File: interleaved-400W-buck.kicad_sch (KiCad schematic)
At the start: 3 parts, among them U1 STM32G474CBTx, U2 TCAN330, U3 LTC7891RUFDM

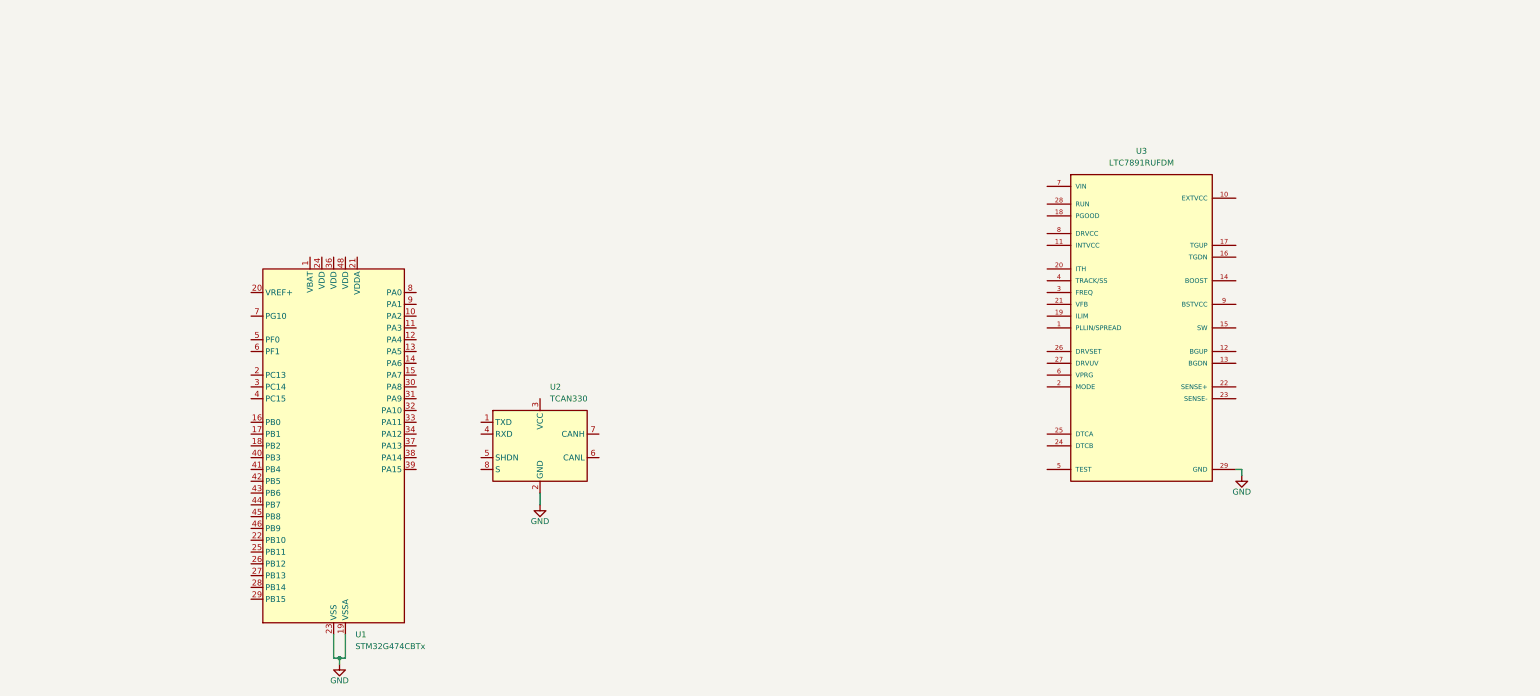
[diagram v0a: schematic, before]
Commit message: Update interleaved-400W-buck.kicad_sch
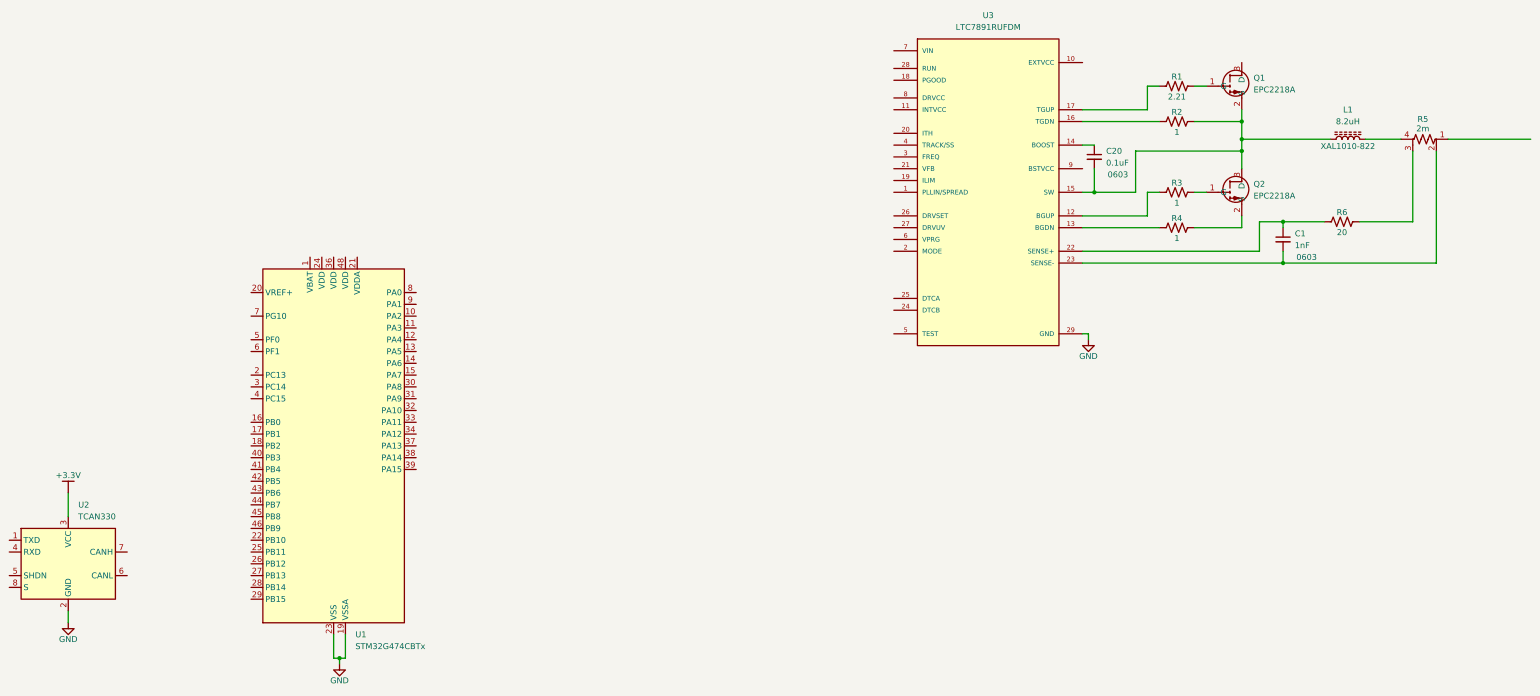
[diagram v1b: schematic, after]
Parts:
- added C1: 1nF, Capacitor_SMD:C_0603_1608Metric_Pad1.08x0.95mm_HandSolder, symbol Device:C_Small
- added C20: 0.1uF, Capacitor_SMD:C_0603_1608Metric_Pad1.08x0.95mm_HandSolder, symbol Device:C_Small
- added L1: 8.2uH, Inductor_SMD:L_Coilcraft_XAL1010-XXX, symbol Device:L_Ferrite
- added Q1, Q2: EPC2218A, jannett_footprints:TRANS_EPC2218A, symbol jannett_symbols:EPC2218A
- added R1: 2.21, Resistor_SMD:R_1206_3216Metric, symbol Device:R_US
- added R2, R3, R4: 1, Resistor_SMD:R_1206_3216Metric, symbol Device:R_US
- added R5: 2m, Resistor_SMD:R_Shunt_Vishay_WSK2512_6332Metric_T2.21mm, symbol Device:R_Shunt_US
- added R6: 20, Resistor_SMD:R_1206_3216Metric, symbol Device:R_US
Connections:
- net at U3.12 (BGUP): now also R3.2
- net at U3.13 (BGDN): now also R4.2
- net at U3.14 (BOOST): now also C20.1
- net at U3.15 (SW): now also C20.2, L1.1, Q1.2 (S), Q1.4 (S), Q1.6 (S), Q1.8 (S), Q2.3 (D), Q2.5 (D), Q2.7 (D), R2.1
- net at U3.16 (TGDN): now also R2.2
- net at U3.17 (TGUP): now also R1.2
- net at U3.22 (SENSE+): now also C1.1, R6.2
- net at U3.23 (SENSE-): now also C1.2, R5.2
- net +3.3V: now reaches U2.3 (VCC)
- new net: Q1.1 (G), R1.1
- new net: Q1.3 (D), Q1.5 (D), Q1.7 (D)
- new net: Q2.1 (G), R3.1
- new net: R5.3, R6.1
- new net: Q2.2 (S), Q2.4 (S), Q2.6 (S), Q2.8 (S), R4.1
- new net: L1.2, R5.4
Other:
- moved on the sheet: U2, U3
